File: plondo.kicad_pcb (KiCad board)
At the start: 2 copper layers, 229.9 x 112.2 mm, 137 parts, among them J1 AVR ISP, J2 USB4085, SW0 MX_SW_HS, SW1 MX_SW_HS, SW10 MX_SW_HS, SW11 MX_SW_HS, SW12 MX_SW_HS, SW13 MX_SW_HS, SW14 MX_SW_HS, SW15 MX_SW_HS, SW16 MX_SW_HS, SW17 MX_SW_HS, SW18 MX_SW_HS, SW19 MX_SW_HS, SW2 MX_SW_HS, SW20 MX_SW_HS, SW21 MX_SW_HS, SW22 MX_SW_HS, SW23 MX_SW_HS, SW24 MX_SW_HS, SW25 MX_SW_HS, SW26 MX_SW_HS, SW27 MX_SW_HS, SW28 MX_SW_HS, SW29 MX_SW_HS, SW3 MX_SW_HS, SW30 MX_SW_HS, SW31 MX_SW_HS, SW32 MX_SW_HS, SW33 MX_SW_HS, SW34 MX_SW_HS, SW35 MX_SW_HS, SW36 MX_SW_HS, SW37 MX_SW_HS, SW38 MX_SW_HS, SW39 MX_SW_HS, SW4 MX_SW_HS, SW40 MX_SW_HS, SW41 MX_SW_HS, SW42 MX_SW_HS, SW43 MX_SW_HS, SW44 MX_SW_HS, SW45 MX_SW_HS, SW46 MX_SW_HS, SW47 MX_SW_HS, SW5 MX_SW_HS, SW6 MX_SW_HS, SW7 MX_SW_HS, SW8 MX_SW_HS, SW9 MX_SW_HS, U1 ATmega32A-P, Y1 16MHz

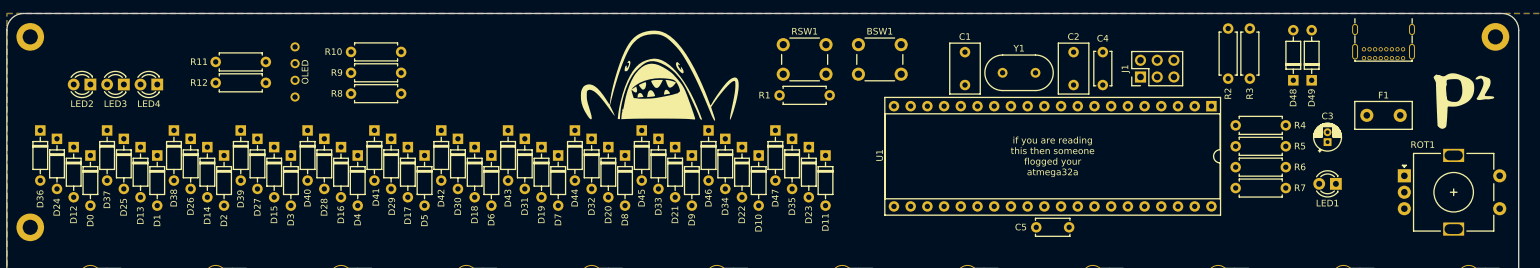
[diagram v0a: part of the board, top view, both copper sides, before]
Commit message: route most everything that isn't the key matrix
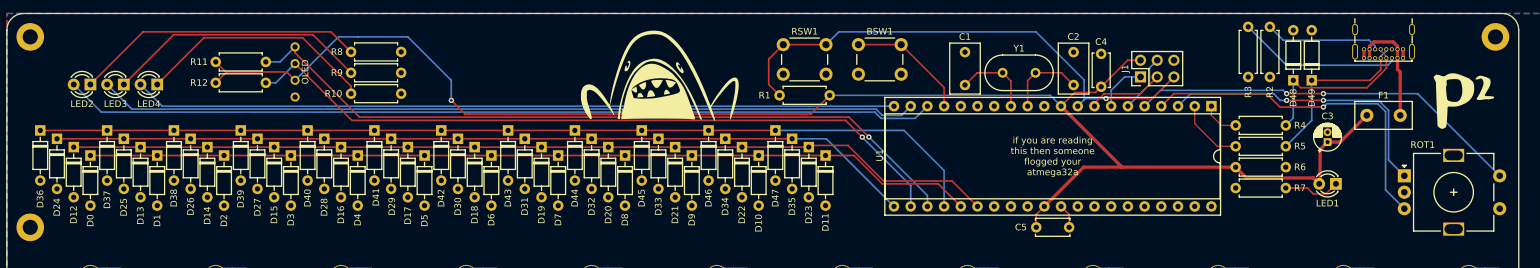
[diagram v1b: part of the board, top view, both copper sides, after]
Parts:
- moved R2 6.36 mm to (220.0, 32.5)
- moved R10 6.35 mm to (87.9, 42.7)
- moved R8 6.35 mm to (87.9, 36.3)
- moved C4 5.26 mm to (194.3, 41.6), turned to 90 degrees
- moved R3 0.36 mm to (216.7, 40.1)
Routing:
- net VCC: track 0.00 -> 234.9 mm, vias 0 -> 1
- net ROW4: track 0.00 -> 145.4 mm
- net ROW2: track 0.00 -> 141.4 mm
- net ROW1: track 0.00 -> 135.5 mm
- net IND1: track 0.00 -> 132.7 mm
- net ROW3: track 0.00 -> 131.5 mm
- net IND2: track 0.00 -> 124.7 mm
- net IND3: track 0.00 -> 115.9 mm
- net SDA: track 0.00 -> 113.1 mm, vias 0 -> 1
- net SCL: track 0.00 -> 110.1 mm, vias 0 -> 1
- net RESET: track 0.00 -> 78.4 mm, vias 0 -> 1
- net ROW0: track 0.00 -> 60.4 mm, vias 0 -> 2
- net ROT_B: track 0.00 -> 52.4 mm, vias 0 -> 1
- net ROT_A: track 0.00 -> 44.8 mm, vias 0 -> 2
- net Net-(LED2-Pad1): track 0.00 -> 44.2 mm
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
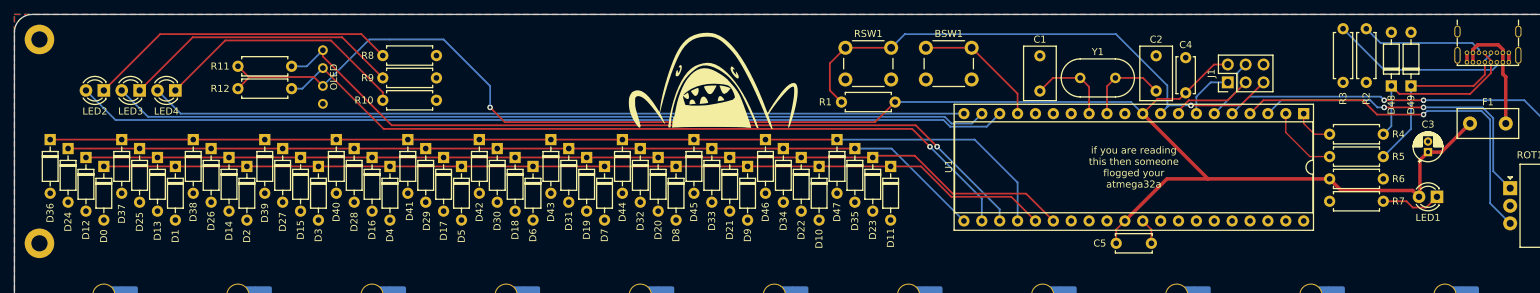
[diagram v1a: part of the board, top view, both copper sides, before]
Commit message: move some components around
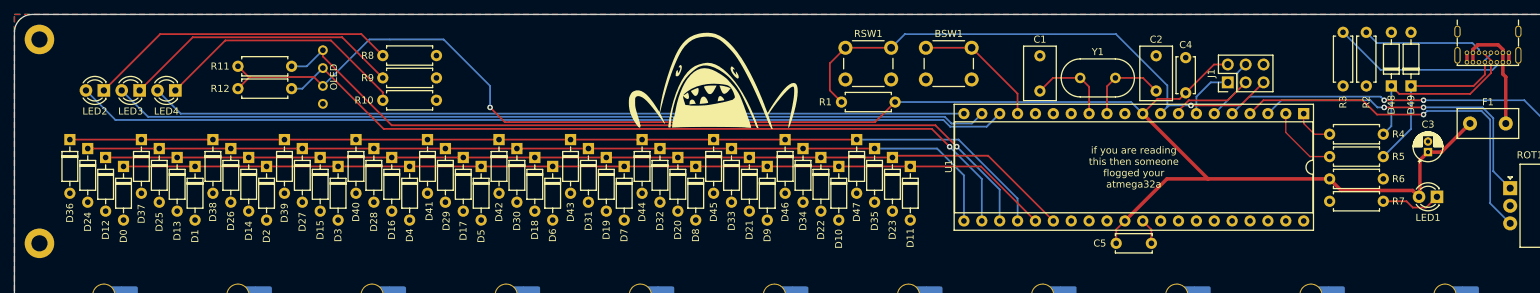
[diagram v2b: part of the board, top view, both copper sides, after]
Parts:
- moved D16 2.79 mm to (81.5, 50.8)
- moved D20 2.79 mm to (122.2, 50.8)
- moved D21 2.79 mm to (132.3, 50.8)
- moved D22 2.79 mm to (142.5, 50.8)
- moved D33 2.79 mm to (129.8, 49.5)
- moved D34 2.79 mm to (140.0, 49.5)
- moved D35 2.79 mm to (150.1, 49.5)
- moved D41 2.79 mm to (86.6, 48.3)
- moved D45 2.79 mm to (127.3, 48.3)
- moved D47 2.79 mm to (147.6, 48.3)
- moved D6 2.79 mm to (104.4, 52.1)
- moved D1 2.79 mm to (53.6, 52.1)
- moved D13 2.79 mm to (51.1, 50.8)
- moved D25 2.79 mm to (48.5, 49.5)
- moved D0 2.79 mm to (43.4, 52.1)
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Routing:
- net ROW4: track 145.4 -> 141.3 mm
- net ROW2: track 141.4 -> 138.6 mm
- net ROW1: track 135.5 -> 132.7 mm
- net SDA: track 113.1 -> 114.7 mm
- net SCL: track 110.1 -> 111.7 mm
- net ROW3: track 131.5 -> 132.5 mm

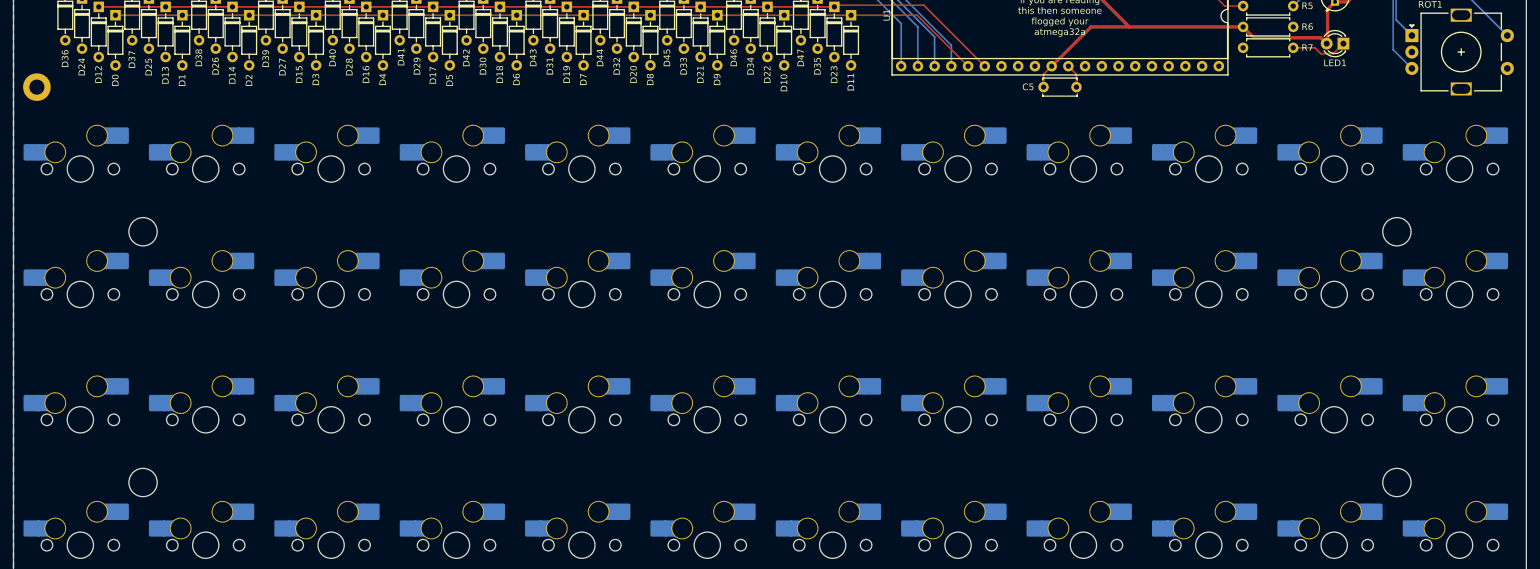
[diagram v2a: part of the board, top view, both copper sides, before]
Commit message: connect all diodes
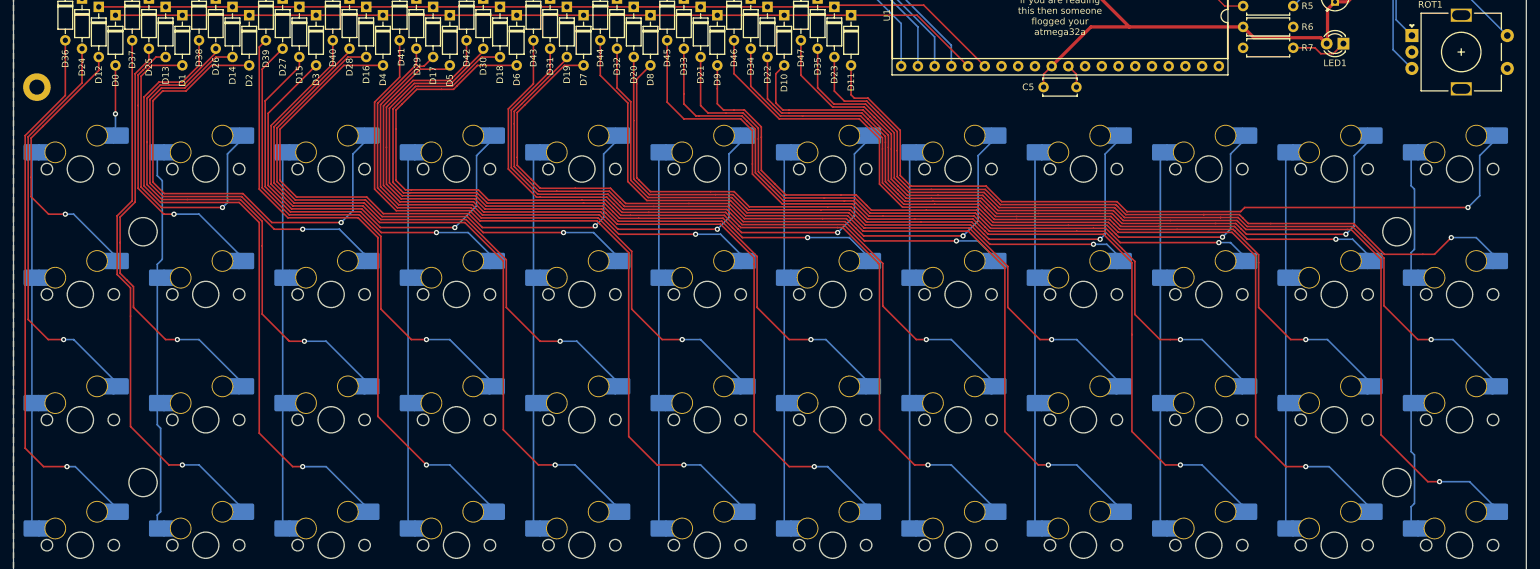
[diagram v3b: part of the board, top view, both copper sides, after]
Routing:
- net Net-(D47-Pad2): track 0.00 -> 158.6 mm, vias 0 -> 1
- net Net-(D46-Pad2): track 0.00 -> 150.0 mm, vias 0 -> 1
- net Net-(D45-Pad2): track 0.00 -> 142.5 mm, vias 0 -> 1
- net Net-(D42-Pad2): track 0.00 -> 140.1 mm, vias 0 -> 1
- net Net-(D35-Pad2): track 0.00 -> 136.6 mm, vias 0 -> 1
- net Net-(D44-Pad2): track 0.00 -> 133.9 mm, vias 0 -> 1
- net Net-(D43-Pad2): track 0.00 -> 131.9 mm, vias 0 -> 1
- net Net-(D34-Pad2): track 0.00 -> 128.0 mm, vias 0 -> 1
- net Net-(D23-Pad2): track 0.00 -> 123.1 mm, vias 0 -> 1
- net Net-(D11-Pad2): track 0.00 -> 122.7 mm, vias 0 -> 1
- net Net-(D10-Pad2): track 0.00 -> 121.9 mm, vias 0 -> 1
- net Net-(D33-Pad2): track 0.00 -> 120.6 mm, vias 0 -> 1
- net Net-(D30-Pad2): track 0.00 -> 120.4 mm, vias 0 -> 1
- net Net-(D6-Pad2): track 0.00 -> 119.2 mm, vias 0 -> 1
- net Net-(D41-Pad2): track 0.00 -> 117.5 mm, vias 0 -> 1
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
